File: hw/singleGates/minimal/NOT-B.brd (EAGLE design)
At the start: 3 parts, among them Q1 BC817

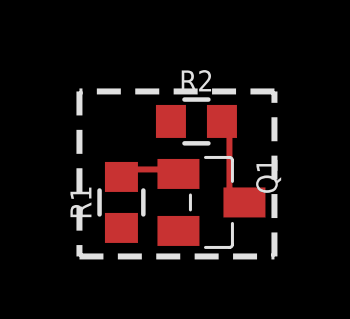
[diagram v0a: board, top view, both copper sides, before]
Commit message: Add led output and prepare first alu slice
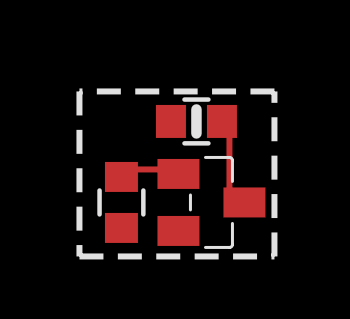
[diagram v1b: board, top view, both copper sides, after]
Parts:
- R2: device p.peter-gator:R0603 -> p.peter-rcl:R0603-MARK
